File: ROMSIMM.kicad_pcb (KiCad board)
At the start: 4 copper layers, 97.8 x 25 mm, 39 parts, among them J1 ROM, SW1 ROM Sel., U1 MX29LV640, U10 74AHC245, U11 XC6206P332MR, U12 74LVC1G02GW, U2 MX29LV640, U3 74AHC245, U4 74AHC245, U5 74AHC245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

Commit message: Update ROMSIMM.kicad_pcb
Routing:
- net /R~WE~: track 53.3 -> 54.4 mm
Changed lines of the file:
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@@
     (thickness 1.6)
     (drawings 46)
-    (tracks 1466)
+    (tracks 1465)
     (zones 0)
     (modules 39)
@@
   (via (at 116.75 110.35) (size 0.508) (drill 0.2) (layers F.Cu B.Cu) (net 7))
   (via (at 115.25 110.35) (size 0.508) (drill 0.2) (layers F.Cu B.Cu) (net 7))
-  (via (at 118.15 110.35) (size 0.508) (drill 0.2) (layers F.Cu B.Cu) (net 7))
+  (via (at 117.55 109.75) (size 0.508) (drill 0.2) (layers F.Cu B.Cu) (net 7))
   (via (at 105.25 108.45) (size 0.508) (drill 0.2) (layers F.Cu B.Cu) (net 7))
   (via (at 107.85 110.35) (size 0.508) (drill 0.2) (layers F.Cu B.Cu) (net 7))
@@
   (segment (start 109.2 109.95) (end 109.95 109.95) (width 0.15) (layer F.Cu) (net 73))
   (segment (start 112.7 116.3) (end 112.7 117.2) (width 0.15) (layer F.Cu) (net 74))
-  (segment (start 113.85 115.15) (end 112.7 116.3) (width 0.15) (layer F.Cu) (net 74))
-  (segment (start 113.85 109) (end 113.85 115.15) (width 0.15) (layer F.Cu) (net 74))
   (segment (start 112.6 107.75) (end 113.85 109) (width 0.15) (layer F.Cu) (net 74))
-  (segment (start 110.65 107.75) (end 112.6 107.75) (width 0.15) (layer F.Cu) (net 74))
+  (segment (start 113.85 109) (end 113.85 115.15) (width 0.15) (layer F.Cu) (net 74))
   (segment (start 109.95 108.45) (end 110.65 107.75) (width 0.15) (layer F.Cu) (net 74))
+  (segment (start 113.85 115.15) (end 112.7 116.3) (width 0.15) (layer F.Cu) (net 74))
+  (segment (start 110.65 107.75) (end 112.6 107.75) (width 0.15) (layer F.Cu) (net 74))
   (segment (start 109.2 108.45) (end 109.95 108.45) (width 0.15) (layer F.Cu) (net 74))
   (segment (start 112.75 107.45) (end 109.2 107.45) (width 0.15) (layer F.Cu) (net 75))
@@
   (segment (start 89.69 108.95) (end 91.5 108.95) (width 0.15) (layer F.Cu) (net 102))
   (via (at 91.5 108.95) (size 0.5) (drill 0.2) (layers F.Cu B.Cu) (net 102))
-  (segment (start 122.8 117.2) (end 122.8 115.5) (width 0.15) (layer F.Cu) (net 102))
-  (segment (start 131.35 108.95) (end 133.45 108.95) (width 0.15) (layer In2.Cu) (net 102))
-  (segment (start 129.15 111.15) (end 131.35 108.95) (width 0.15) (layer In2.Cu) (net 102))
-  (segment (start 124.9 111.15) (end 129.15 111.15) (width 0.15) (layer In2.Cu) (net 102))
+  (via (at 119.25 110.95) (size 0.5) (drill 0.2) (layers F.Cu B.Cu) (net 102))
+  (segment (start 119.25 110.95) (end 124.7 110.95) (width 0.15) (layer In2.Cu) (net 102))
+  (segment (start 117.275 110.95) (end 117.075 111.15) (width 0.15) (layer In2.Cu) (net 102))
   (segment (start 124.7 110.95) (end 124.9 111.15) (width 0.15) (layer In2.Cu) (net 102))
-  (segment (start 121.95 110.95) (end 124.7 110.95) (width 0.15) (layer In2.Cu) (net 102))
-  (via (at 121.95 110.95) (size 0.5) (drill 0.2) (layers F.Cu B.Cu) (net 102))
-  (segment (start 118.5 111.15) (end 93.7 111.15) (width 0.15) (layer In2.Cu) (net 102))
+  (segment (start 124.9 111.15) (end 129.15 111.15) (width 0.15) (layer In2.Cu) (net 102))
+  (segment (start 131.35 108.95) (end 133.45 108.95) (width 0.15) (layer In2.Cu) (net 102))
+  (segment (start 119.25 110.95) (end 117.275 110.95) (width 0.15) (layer In2.Cu) (net 102))
   (segment (start 93.7 111.15) (end 91.5 108.95) (width 0.15) (layer In2.Cu) (net 102))
-  (segment (start 118.7 110.95) (end 118.5 111.15) (width 0.15) (layer In2.Cu) (net 102))
-  (segment (start 121.95 110.95) (end 118.7 110.95) (width 0.15) (layer In2.Cu) (net 102))
-  (segment (start 121.95 114.65) (end 122.8 115.5) (width 0.15) (layer F.Cu) (net 102))
-  (segment (start 121.95 110.95) (end 121.95 114.65) (width 0.15) (layer F.Cu) (net 102))
+  (segment (start 117.075 111.15) (end 93.7 111.15) (width 0.15) (layer In2.Cu) (net 102))
+  (segment (start 129.15 111.15) (end 131.35 108.95) (width 0.15) (layer In2.Cu) (net 102))
+  (segment (start 122.8 114.5) (end 122.8 117.2) (width 0.15) (layer F.Cu) (net 102))
+  (segment (start 119.25 110.95) (end 122.8 114.5) (width 0.15) (layer F.Cu) (net 102))
   (via (at 131.55 112.95) (size 0.5) (drill 0.2) (layers F.Cu B.Cu) (net 103))
   (segment (start 132.49 112.95) (end 131.55 112.95) (width 0.15) (layer F.Cu) (net 103))
@@
   (segment (start 91.7 108.45) (end 88.75 108.45) (width 0.15) (layer In2.Cu) (net 124))
   (segment (start 94.1 110.85) (end 91.7 108.45) (width 0.15) (layer In2.Cu) (net 124))
-  (segment (start 118.35 110.85) (end 94.1 110.85) (width 0.15) (layer In2.Cu) (net 124))
-  (segment (start 118.75 110.45) (end 118.35 110.85) (width 0.15) (layer In2.Cu) (net 124))
-  (segment (start 124.65 110.45) (end 118.75 110.45) (width 0.15) (layer In2.Cu) (net 124))
+  (segment (start 116.95 110.85) (end 94.1 110.85) (width 0.15) (layer In2.Cu) (net 124))
+  (segment (start 117.35 110.45) (end 116.95 110.85) (width 0.15) (layer In2.Cu) (net 124))
+  (segment (start 124.65 110.45) (end 117.35 110.45) (width 0.15) (layer In2.Cu) (net 124))
   (segment (start 125.05 110.85) (end 124.65 110.45) (width 0.15) (layer In2.Cu) (net 124))
-  (segment (start 131.4 108.45) (end 129 110.85) (width 0.15) (layer In2.Cu) (net 124))
   (segment (start 129 110.85) (end 125.05 110.85) (width 0.15) (layer In2.Cu) (net 124))
+  (segment (start 131.4 108.45) (end 129 110.85) (width 0.15) (layer In2.Cu) (net 124))
   (segment (start 131.55 108.45) (end 131.4 108.45) (width 0.15) (layer In2.Cu) (net 124))
   (zone (net 7) (net_name GND) (layer F.Cu) (hatch edge 0.508)

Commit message: Start on triple DIP switch
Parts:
- added R1: 3k3, stdpads:R_0603, F.Cu at (159.7, 104.4)
- added SW1: ROM Sel., stdpads:SW_DIP_SPSTx02_Slide_DSHP02TS_P1.27mm, F.Cu at (158.0, 110.9)
- moved FID4 2.92 mm to (162.4, 104.3)
- moved R1 1.40 mm to (156.8, 104.4)
- moved R2 0.99 mm to (154.8, 105.1), turned to 90 degrees
- moved SW1 0.25 mm to (159.3, 110.9)
- moved C5 0.20 mm to (154.3, 109.5)
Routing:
- net /RA23: track 95.7 -> 89.4 mm, vias 3 -> 2
- net /RD29: track 14.3 -> 9.72 mm
- net /RD28: track 14.2 -> 9.74 mm
- net /RA22sw: track 79.4 -> 75.4 mm, vias 3 -> 2
- net +3V3: track 58.2 -> 55.0 mm, vias 75 -> 74
- net /RD30: track 14.9 -> 12.1 mm
- net /RD31: track 15.6 -> 13.8 mm
- net GND: track 84.9 -> 84.1 mm, vias 153 -> 152
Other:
- board text added: "IIsi"
- board text added: "IIx"
- board text added: "ROM"
- board text removed: "ROM Disk"
- board text removed: "none"

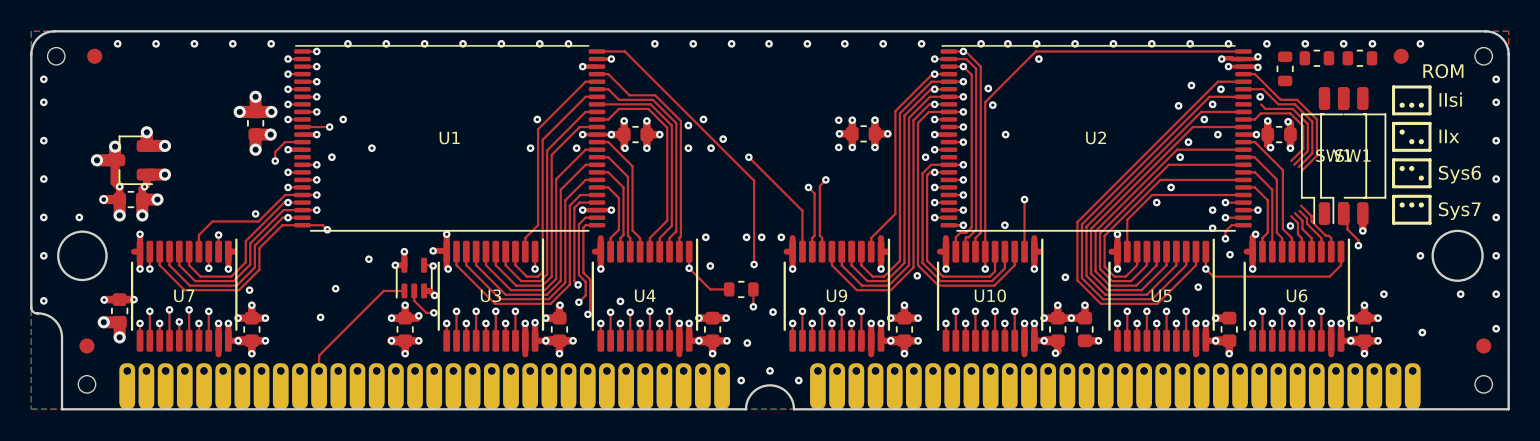
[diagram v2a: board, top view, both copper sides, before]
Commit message: Migrate to KiCAD 6
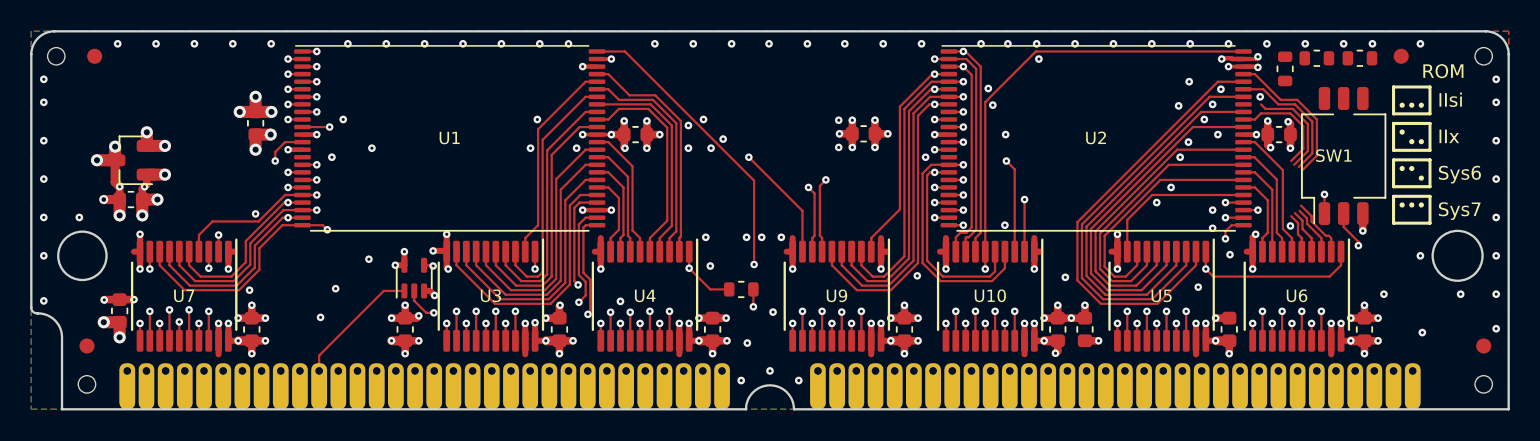
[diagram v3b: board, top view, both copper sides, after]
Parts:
- removed the SW1 at (158.0, 110.9)
- removed the SW1 at (159.3, 110.9)
- added SW1: ROM Sel., stdpads:SW_DIP_SPSTx03_Slide_DSHP03TS_P1.27mm, F.Cu at (158.6, 110.9)
- renumbered R1 to R4
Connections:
- net /R~CS~ renamed /R~{CS}
- net /R~OE~ renamed /R~{OE}
- net /R~WE~ renamed /R~{WE}
- net /~CS~ renamed /~{CS}
- net /~OE~ renamed /~{OE}
- net /~WE~ renamed /~{WE}
- R1 pad 1: /RA23 -> /RA22sw
- R2 pad 1: /RA22sw -> /RA23
- R4 pad 1: /RA23 -> /RA21sw
- U1 pad 9: /RA21 -> /RA21sw
- U2 pad 9: /RA21 -> /RA21sw
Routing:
- net /RA21sw: track 0.00 -> 69.8 mm, vias 0 -> 2
- net /RA21: track 64.9 -> 29.5 mm
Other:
- net class Default removed
- board text added: "4402C"
- board text removed: "4402B"

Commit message: Done?
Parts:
- turned U12 to -90 degrees
- renumbered R4 to R1, R1 to R2, R2 to R4
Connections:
- J1 pad 63: Net-(J1-Pad63) -> unconnected-(J1-Pad63)
- R1 pad 1: /RA21sw -> /RA22sw
- R2 pad 1: /RA22sw -> /RA23
- R4 pad 1: /RA23 -> /RA21sw
- U1 pad 15: Net-(U1-Pad15) -> unconnected-(U1-Pad15)
- U2 pad 15: Net-(U2-Pad15) -> unconnected-(U2-Pad15)
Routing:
- net /RA22sw: track 75.4 -> 80.2 mm, vias 2 -> 3
- net /RD29: track 9.72 -> 14.3 mm
- net /RA23: track 89.4 -> 93.9 mm, vias 2 -> 3
- net /RA21sw: track 69.8 -> 74.2 mm, vias 2 -> 3
- net /RD28: track 9.74 -> 13.7 mm
- net +3V3: track 55.0 -> 58.2 mm
- net /RD30: track 12.1 -> 15.2 mm
- net /RD31: track 13.8 -> 16.3 mm
